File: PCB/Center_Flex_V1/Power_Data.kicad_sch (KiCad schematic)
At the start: 80 parts, among them J100 Conn_01x01_Pin, J101 Conn_01x01_Pin, J102 Conn_01x01_Pin, J103 Conn_01x01_Pin, J104 Conn_01x01_Pin, J105 Conn_01x01_Pin, J106 Conn_01x01_Pin, J107 Conn_01x01_Pin, J108 Conn_01x01_Pin, J109 Conn_01x01_Pin, J11 Conn_01x01_Socket, J110 Conn_01x01_Pin, J111 Conn_01x01_Pin, J112 Conn_01x01_Pin, J113 Conn_01x02_Socket, J114 Conn_01x02_Pin, J115 Conn_01x02_Pin, J116 Conn_01x02_Socket, J117 Conn_01x02_Pin, J118 Conn_01x02_Socket, J119 Conn_01x02_Pin, J12 Conn_01x01_Pin, J120 Conn_01x02_Socket, J17 Conn_01x02_Socket, J20 Conn_01x01_Pin, J23 Conn_01x01_Socket, J24 Conn_01x01_Pin, J31 Conn_01x01_Socket, J34 Conn_01x01_Socket, J39 Conn_01x01_Socket, J40 Conn_01x01_Socket, J41 Conn_01x01_Socket, J46 Conn_01x01_Socket, J47 Conn_01x01_Socket, J5 Conn_01x02_Socket, J50 Conn_01x01_Socket, J53 Conn_01x01_Socket, J56 Conn_01x01_Socket, J59 Conn_01x01_Socket, J60 Conn_01x01_Socket, J61 Conn_01x01_Socket, J62 Conn_01x01_Socket, J63 Conn_01x01_Socket, J64 Conn_01x01_Socket, J65 Conn_01x01_Socket, J66 Conn_01x01_Socket, J67 Conn_01x01_Socket, J68 Conn_01x01_Socket, J69 Conn_01x01_Socket, J70 Conn_01x01_Socket, J71 Conn_01x01_Socket, J72 Conn_01x01_Socket, J73 Conn_01x01_Socket, J74 Conn_01x01_Socket, J75 Conn_01x01_Socket, J76 Conn_01x01_Socket, J77 Conn_01x01_Socket, J78 Conn_01x01_Socket, J79 Conn_01x01_Socket, J8 Conn_01x01_Pin, J80 Conn_01x01_Socket, J81 Conn_01x01_Socket, J82 Conn_01x01_Socket, J83 Conn_01x01_Pin, J84 Conn_01x01_Pin, J85 Conn_01x01_Pin, J86 Conn_01x01_Pin, J87 Conn_01x01_Pin, J88 Conn_01x01_Pin, J89 Conn_01x01_Pin, J90 Conn_01x01_Pin, J91 Conn_01x01_Pin, J92 Conn_01x01_Pin, J93 Conn_01x01_Pin, J94 Conn_01x01_Pin, J95 Conn_01x01_Pin, J96 Conn_01x01_Pin, J97 Conn_01x01_Pin, J98 Conn_01x01_Pin, J99 Conn_01x01_Pin

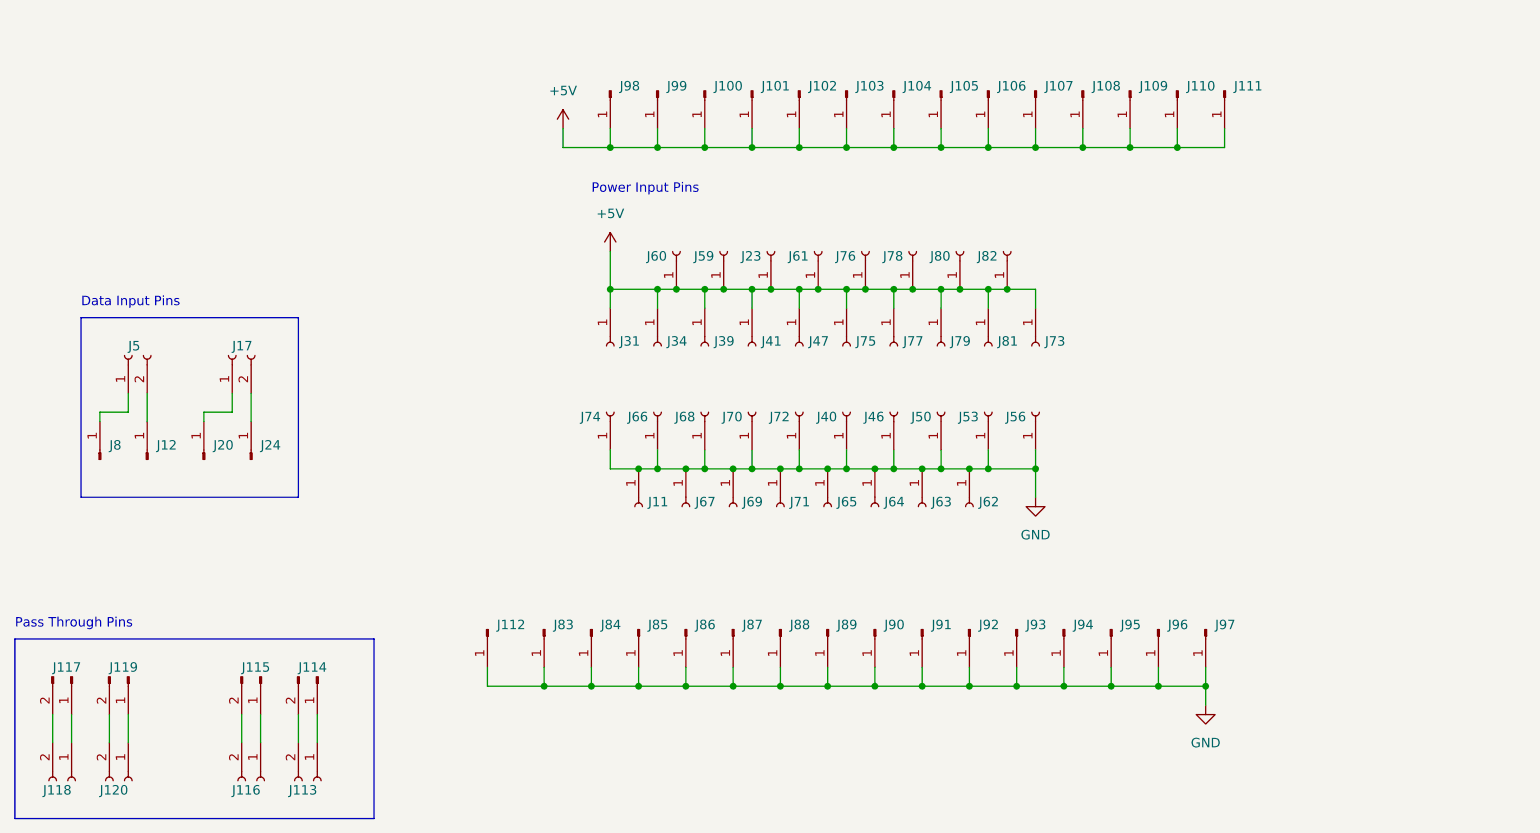
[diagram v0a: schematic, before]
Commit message: Flex PCBs ordered
All Flex PCBs are finalized and ordered
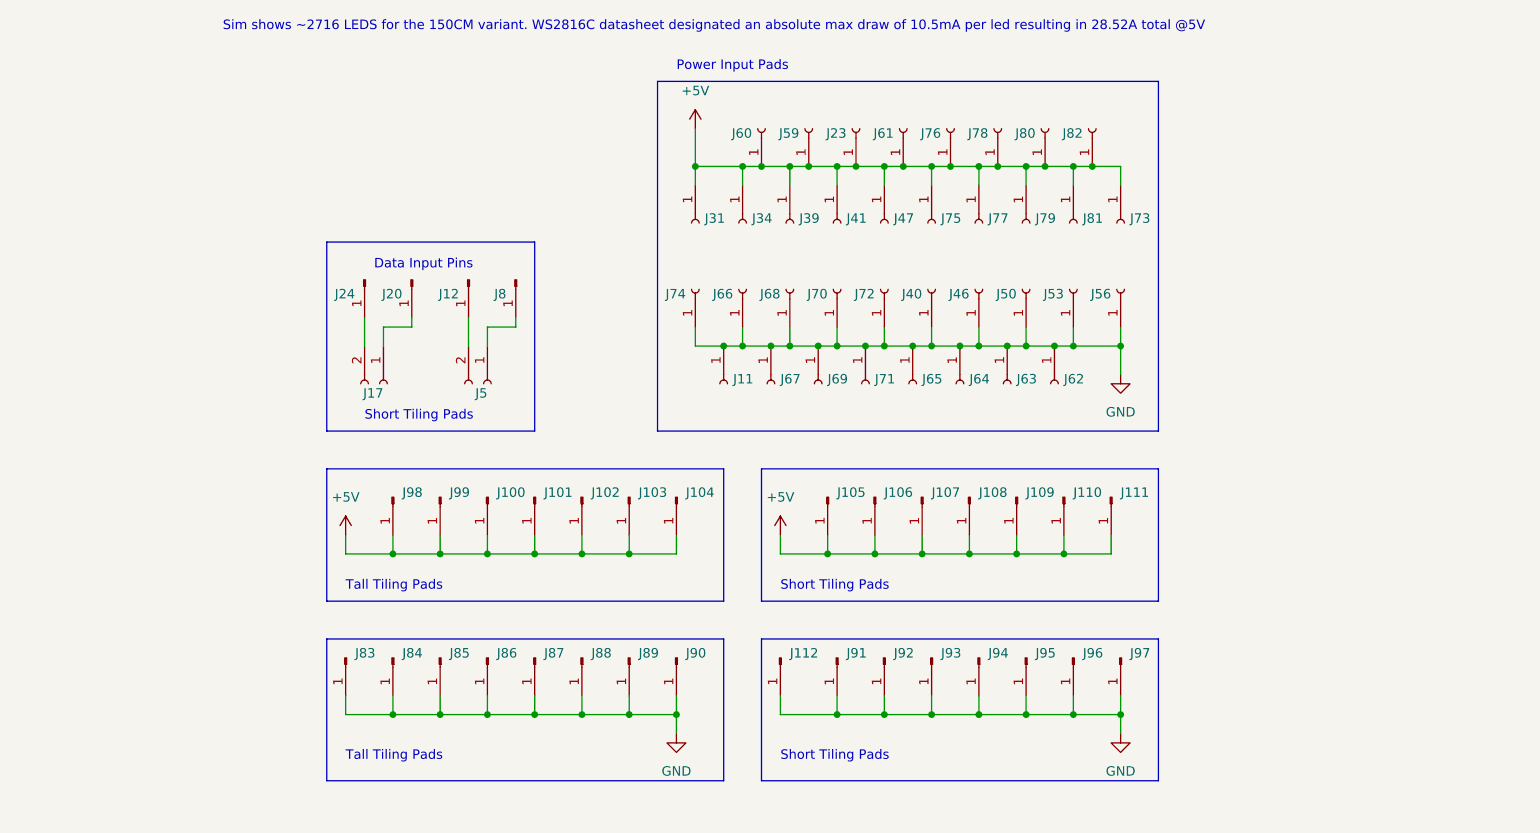
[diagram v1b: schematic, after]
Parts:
- removed J113, J116, J118, J120: Conn_01x02_Socket, Dustins_Footprints:Snowboard_Flex_Solder_Pad, symbol Connector:Conn_01x02_Socket
- removed J114, J115, J117, J119: Conn_01x02_Pin, Dustins_Footprints:Snowboard_Flex_Solder_Pad, symbol Connector:Conn_01x02_Pin
- J105, J106, J107, J108, J109, J110, J111, J112, J91, J92, J93, J94, J95, J96, J97: footprint Dustins_Footprints:SnowBoard Power Pads -> Dustins_Footprints:SnowBoard Power Pads Short
- J17, J5: footprint Dustins_Footprints:SnowBoard Flex Pass Through Pads -> Dustins_Footprints:SnowBoard Flex Pass Through Pads Short
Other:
- note added: "Power Input Pads"
- note added: "Short Tiling Pads"
- note added: "Sim shows ~2716 LEDS for the 150CM variant. WS2816C datasheet designated an absolute max draw of 10.5mA per led resulting in 28.52A total @5V"
- note added: "Tall Tiling Pads"
- note removed: "Pass Through Pins"
- note removed: "Power Input Pins"
- moved on the sheet: J100, J101, J102, J103, J104, J105, J106, J107, J108, J109, J11, J110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
